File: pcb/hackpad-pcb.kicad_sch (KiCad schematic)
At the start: 50 parts, among them J1 OLED_128x32, U1 MCU_Seeed_XIAO_RP2040

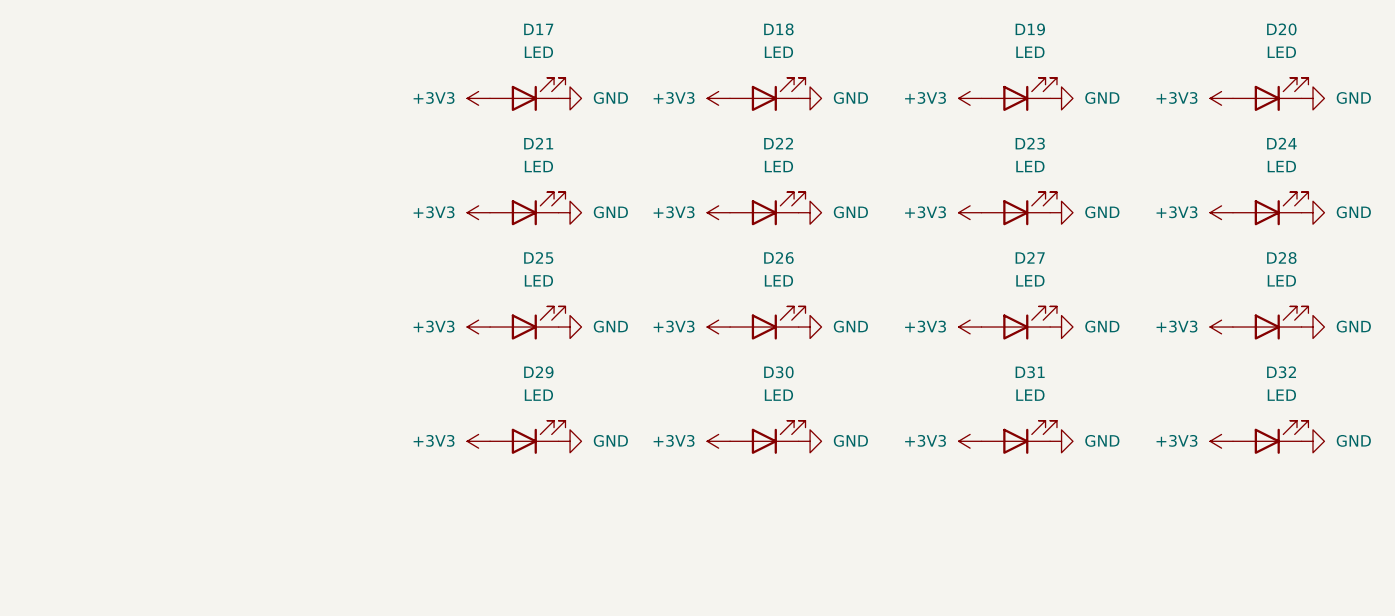
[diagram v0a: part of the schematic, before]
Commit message: Add resistors for LEDs
Signed-off-by: Urjith Mishra <66270347+TheScientist101@users.noreply.github.com>
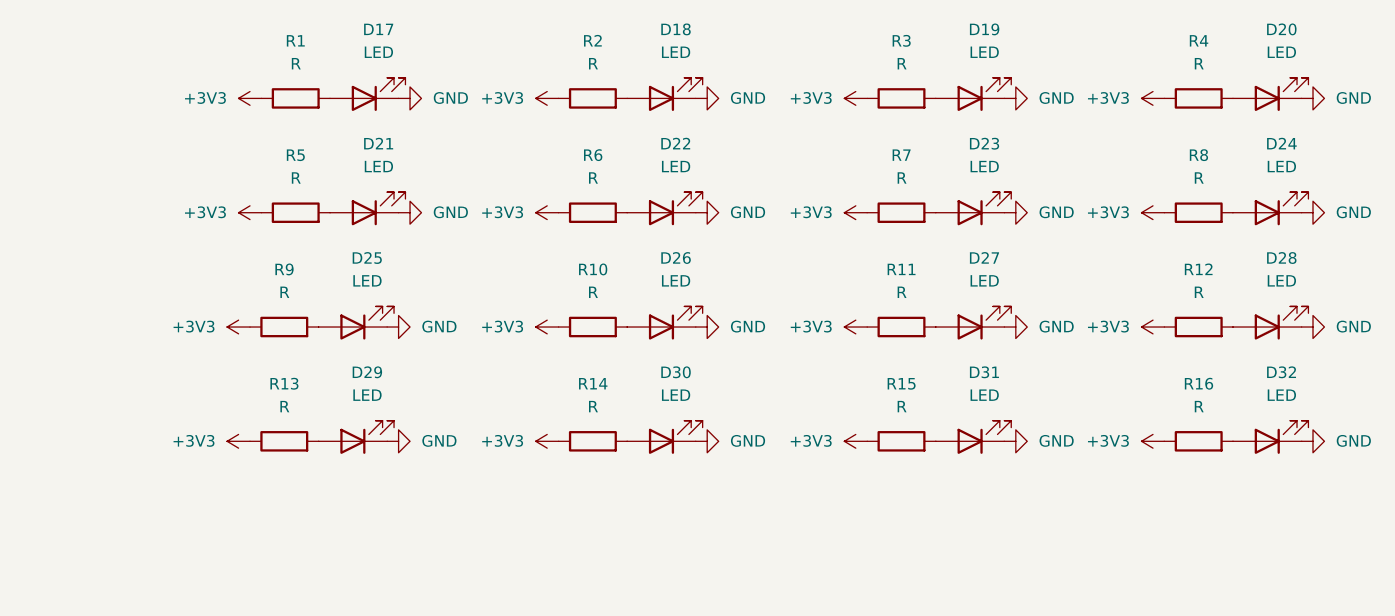
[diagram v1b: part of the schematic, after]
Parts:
- added R1, R10, R11, R12, R13, R14, R15, R16, R2, R3, R4, R5, R6, R7, R8, R9: R, Resistor_THT:R_Axial_DIN0207_L6.3mm_D2.5mm_P7.62mm_Horizontal, symbol Device:R
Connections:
- net +3V3: now also R1.1, R10.1, R11.1, R12.1, R13.1, R14.1, R15.1, R16.1, R2.1, R3.1, R4.1, R5.1, R6.1, R7.1, R8.1, R9.1; no longer D17.2 (A), D18.2 (A), D19.2 (A), D20.2 (A), D21.2 (A), D22.2 (A), D23.2 (A), D24.2 (A), D25.2 (A), D26.2 (A), D27.2 (A), D28.2 (A), D29.2 (A), D30.2 (A), D31.2 (A), D32.2 (A)
- new net: D29.2 (A), R13.2
- new net: D21.2 (A), R5.2
- new net: D27.2 (A), R11.2
- new net: D28.2 (A), R12.2
- new net: D19.2 (A), R3.2
- new net: D20.2 (A), R4.2
- new net: D18.2 (A), R2.2
- new net: D30.2 (A), R14.2
- new net: D32.2 (A), R16.2
- new net: D17.2 (A), R1.2
- new net: D26.2 (A), R10.2
- new net: D25.2 (A), R9.2
- new net: D24.2 (A), R8.2
- new net: D23.2 (A), R7.2
- new net: D31.2 (A), R15.2
- new net: D22.2 (A), R6.2
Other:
- moved on the sheet: D17, D18, D19, D21, D22, D23, D25, D26, D27, D29, D30, D31
